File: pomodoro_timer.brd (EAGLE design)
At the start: 83.5 x 44.4 mm, 17 parts

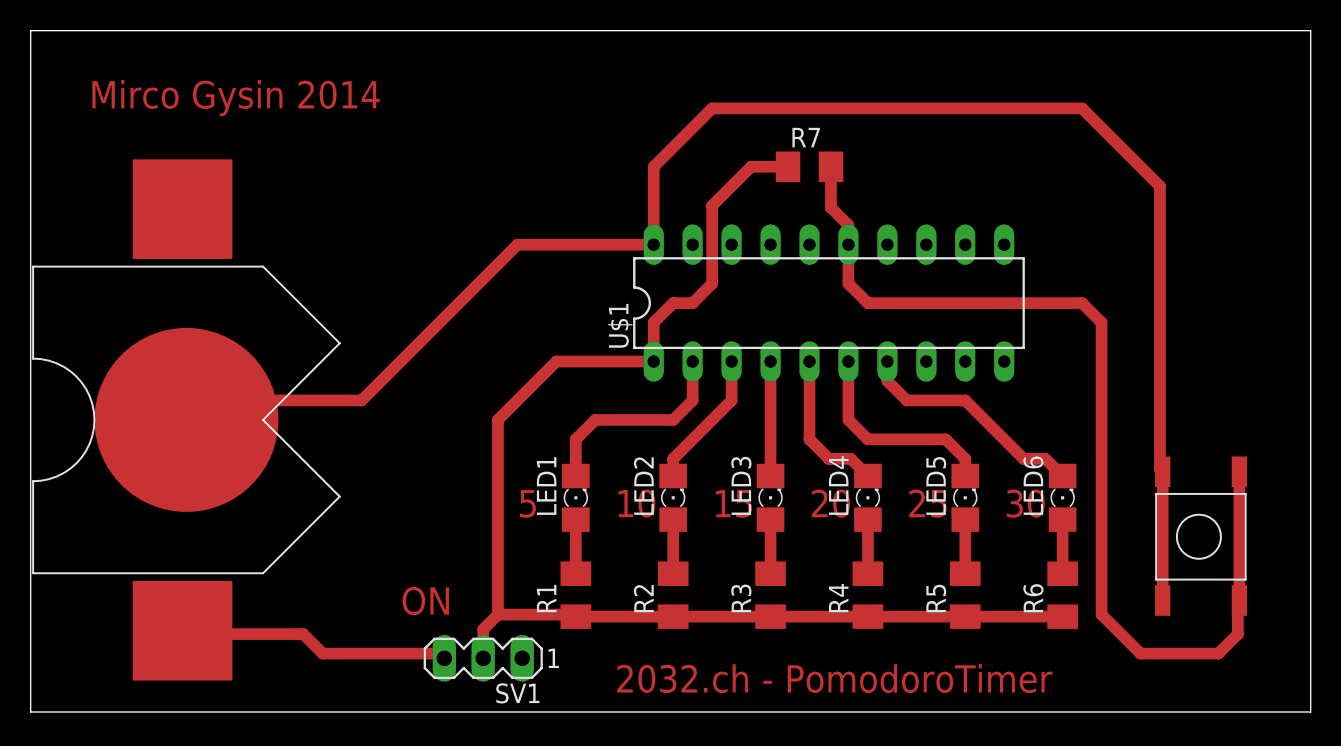
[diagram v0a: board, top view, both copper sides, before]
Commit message: added ground plane + jumper for test input
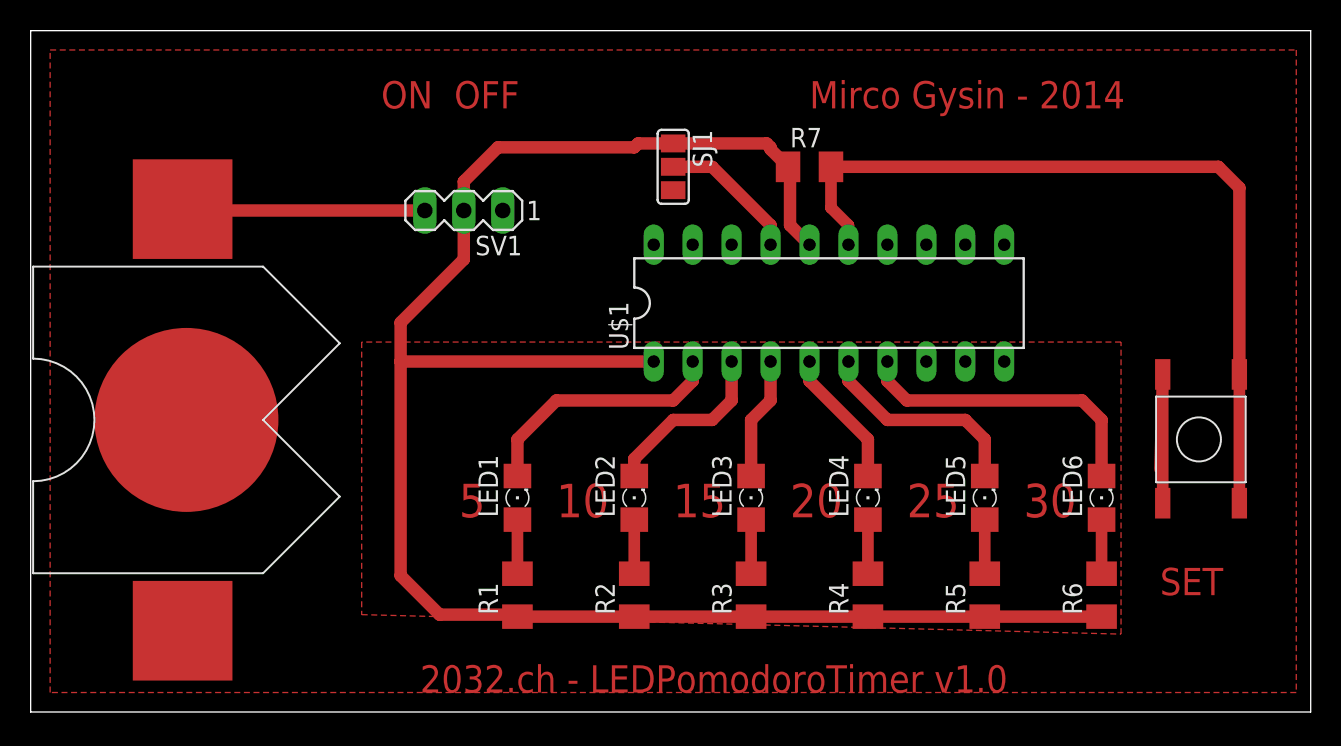
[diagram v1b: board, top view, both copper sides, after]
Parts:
- added SJ1: test_jpr, jumper:SJ_2
- R1, R2, R3, R4, R5, R6: value (none) -> 510
- R7: value (none) -> 100k
- SV1: value (none) -> pwr_switch
- moved SV1 29.2 mm to (28.2, 32.7)
- moved U$3 6.35 mm to (76.2, 17.8)
- moved LED1 3.81 mm to (31.8, 14.0)
- moved R1 3.81 mm to (31.8, 7.62)
- moved LED2 2.54 mm to (39.4, 14.0)
- moved R2 2.54 mm to (39.4, 7.62)
- moved LED6 2.54 mm to (69.8, 14.0)
- moved R6 2.54 mm to (69.8, 7.62)
- moved LED3 1.27 mm to (47.0, 14.0)
- moved LED5 1.27 mm to (62.2, 14.0)
- moved R3 1.27 mm to (47.0, 7.62)
- moved R5 1.27 mm to (62.2, 7.62)
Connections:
- removed net N$1: SV1.3, U$2.P$1, U$2.P$2
- new net N$15: SJ1.2, U$1.17
- new net POS_BAT: SV1.3, U$2.POSITIVE_PAD_1, U$2.POSITIVE_PAD_2
- net GND: now also SJ1.3
- net VCC: now also SJ1.1, U$1.16
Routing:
- net GND: track 104.1 -> 14.6 mm
- net VCC: track 83.1 -> 119.3 mm
- net N$1: track 17.5 -> 0.00 mm
- net POS_BAT: track 0.00 -> 15.7 mm
- net N$14: track 65.8 -> 53.3 mm
- net N$15: track 0.00 -> 9.20 mm
- net N$13: track 15.3 -> 20.0 mm
- net N$2: track 13.6 -> 16.7 mm
- net N$9: track 9.05 -> 11.6 mm
- net N$11: track 9.88 -> 9.05 mm
- net N$12: track 13.6 -> 14.1 mm
- net N$10: track 7.47 -> 7.99 mm
- added copper zone on layer 1, net GND
- added copper zone on layer 1, net N$1
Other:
- board text added: "2032.ch - LEDPomodoroTimer v1.0"
- board text added: "Mirco Gysin - 2014"
- board text added: "ON OFF"
- board text added: "SET"
- board text removed: "2032.ch - PomodoroTimer"
- board text removed: "Mirco Gysin 2014"
- board text removed: "ON"
